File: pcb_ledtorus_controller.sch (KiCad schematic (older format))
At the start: 27 parts, among them P7 CONN_4X2, P8 CONN_9, U1 TM4C1232XXPM, U3 KNUSB, X1 NX5032GA-16MHz

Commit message: Passing ERC
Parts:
- renumbered C16 to C1, C9 to C10, C10 to C11, C11 to C12, C12 to C13, C1 to C2, C2 to C3, C3 to C4, C4 to C5, C5 to C6, C6 to C7, C7 to C8, C8 to C9, P7 to P1, P8 to P2, R6 to R1, R1 to R2, R7 to R3, R17 to R4, R8 to R5
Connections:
- net labels added: +3V3, gpio1, gpio2
- net labels removed: +3.3V, +3.3v, blank3, gnd, gsclk1, gsclk2, gsclk3, hall2, hall3, mode1, mode2, mode3, sclk3, sin2, sout2, sout3, xlat3
- wire segments 144 -> 134
- no-connect marks 1 -> 15
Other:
- moved on the sheet: B1, C1, C10, C11, C12, C13, C2, C3, C4, C5, C6, C7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

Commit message: Starting on netlist
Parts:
- B1: footprint (none) -> knielsenlib:SWITCH_FSMJSMA
- C1, C12, C13, C7, C8, C9: footprint (none) -> Capacitors_SMD:C_0805
- C10, C11, C2, C3, C4, C5, C6: footprint (none) -> Capacitors_SMD:C_0603
- D1, D2: footprint (none) -> LEDs:LED_0805
- L1: footprint (none) -> Inductors_SMD:L_0603
- P1: footprint (none) -> Pin_Headers:Pin_Header_Straight_2x04_Pitch1.27mm
- P2: footprint (none) -> Pin_Headers:Pin_Header_Straight_1x09_Pitch1.27mm
- R1, R2, R3, R4, R5: footprint (none) -> Resistors_SMD:R_0805
- U1: footprint (none) -> knielsenlib:LQFP_64
- U3: footprint (none) -> knielsenlib:10103594-0001LF
- X1: footprint (none) -> knielsenlib:NX5032GA
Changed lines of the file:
@@
 LIBS:w_device
 LIBS:pcb_ledtorus_controller-cache
-LIBS:tiva_pcb1-cache
 EELAYER 26 0
 EELAYER END
@@
 F 0 "R2" V 4630 1550 50  0000 C CNN
 F 1 "10k" V 4550 1550 40  0000 C CNN
-F 2 "" H 4550 1550 60  0001 C CNN
+F 2 "Resistors_SMD:R_0805" H 4550 1550 60  0001 C CNN
 F 3 "" H 4550 1550 60  0001 C CNN
 	1    4550 1550
@@
 F 0 "C7" H 8100 2400 50  0000 L CNN
 F 1 "10u" H 8100 2200 50  0000 L CNN
-F 2 "" H 8050 2300 60  0001 C CNN
+F 2 "Capacitors_SMD:C_0805" H 8050 2300 60  0001 C CNN
 F 3 "" H 8050 2300 60  0001 C CNN
 	1    8050 2300
@@
 F 0 "C6" H 7800 2400 50  0000 L CNN
 F 1 "100n" H 7800 2200 50  0000 L CNN
-F 2 "" H 7750 2300 60  0001 C CNN
+F 2 "Capacitors_SMD:C_0603" H 7750 2300 60  0001 C CNN
 F 3 "" H 7750 2300 60  0001 C CNN
 	1    7750 2300
@@
 F 0 "C2" H 6600 2400 50  0000 L CNN
 F 1 "100n" H 6600 2200 50  0000 L CNN
-F 2 "" H 6550 2300 60  0001 C CNN
+F 2 "Capacitors_SMD:C_0603" H 6550 2300 60  0001 C CNN
 F 3 "" H 6550 2300 60  0001 C CNN
 	1    6550 2300
@@
 F 0 "C3" H 6900 2400 50  0000 L CNN
 F 1 "100n" H 6900 2200 50  0000 L CNN
-F 2 "" H 6850 2300 60  0001 C CNN
+F 2 "Capacitors_SMD:C_0603" H 6850 2300 60  0001 C CNN
 F 3 "" H 6850 2300 60  0001 C CNN
 	1    6850 2300
@@
 F 0 "C4" H 7200 2400 50  0000 L CNN
 F 1 "100n" H 7200 2200 50  0000 L CNN
-F 2 "" H 7150 2300 60  0001 C CNN
+F 2 "Capacitors_SMD:C_0603" H 7150 2300 60  0001 C CNN
 F 3 "" H 7150 2300 60  0001 C CNN
 	1    7150 2300
@@
 F 0 "C5" H 7500 2400 50  0000 L CNN
 F 1 "100n" H 7500 2200 50  0000 L CNN
-F 2 "" H 7450 2300 60  0001 C CNN
+F 2 "Capacitors_SMD:C_0603" H 7450 2300 60  0001 C CNN
 F 3 "" H 7450 2300 60  0001 C CNN
 	1    7450 2300
@@
 F 0 "C13" H 7150 3050 50  0000 L CNN
 F 1 "2.2u" H 7150 2850 50  0000 L CNN
-F 2 "" H 7100 2950 60  0001 C CNN
+F 2 "Capacitors_SMD:C_0805" H 7100 2950 60  0001 C CNN
 F 3 "" H 7100 2950 60  0001 C CNN
 	1    7100 2950
@@
 F 0 "C12" H 6850 3050 50  0000 L CNN
 F 1 "1u" H 6850 2850 50  0000 L CNN
-F 2 "" H 6800 2950 60  0001 C CNN
+F 2 "Capacitors_SMD:C_0805" H 6800 2950 60  0001 C CNN
 F 3 "" H 6800 2950 60  0001 C CNN
 	1    6800 2950
@@
 F 0 "C11" H 6550 3050 50  0000 L CNN
 F 1 "100n" H 6550 2850 50  0000 L CNN
-F 2 "" H 6500 2950 60  0001 C CNN
+F 2 "Capacitors_SMD:C_0603" H 6500 2950 60  0001 C CNN
 F 3 "" H 6500 2950 60  0001 C CNN
 	1    6500 2950
@@
 F 0 "C10" H 6250 3050 50  0000 L CNN
 F 1 "100n" H 6250 2850 50  0000 L CNN
-F 2 "" H 6200 2950 60  0001 C CNN
+F 2 "Capacitors_SMD:C_0603" H 6200 2950 60  0001 C CNN
 F 3 "" H 6200 2950 60  0001 C CNN
 	1    6200 2950
@@
 F 0 "C9" H 4600 2800 50  0000 L CNN
 F 1 "10p" H 4600 2600 50  0000 L CNN
-F 2 "" H 4550 2700 60  0001 C CNN
+F 2 "Capacitors_SMD:C_0805" H 4550 2700 60  0001 C CNN
 F 3 "" H 4550 2700 60  0001 C CNN
 	1    4550 2700
@@
 F 0 "C8" H 4000 2800 50  0000 L CNN
 F 1 "10p" H 4000 2600 50  0000 L CNN
-F 2 "" H 3950 2700 60  0001 C CNN
+F 2 "Capacitors_SMD:C_0805" H 3950 2700 60  0001 C CNN
 F 3 "" H 3950 2700 60  0001 C CNN
 	1    3950 2700
@@
 F 0 "X1" H 4250 2350 60  0000 C CNN
 F 1 "NX5032GA-16MHz" H 4250 2050 60  0000 C CNN
-F 2 "" H 4250 2200 60  0001 C CNN
+F 2 "knielsenlib:NX5032GA" H 4250 2200 60  0001 C CNN
 F 3 "" H 4250 2200 60  0001 C CNN
 	1    4250 2200
@@
 F 0 "U1" H 5450 2700 60  0000 C CNN
 F 1 "TM4C1232XXPM" H 5450 1450 60  0000 C CNN
-F 2 "" H 5450 2150 60  0001 C CNN
+F 2 "knielsenlib:LQFP_64" H 5450 2150 60  0001 C CNN
 F 3 "" H 5450 2150 60  0001 C CNN
 	2    5450 2150
@@
 F 0 "U1" H 2250 2800 60  0000 C CNN
 F 1 "TM4C1232XXPM" H 2250 2700 60  0000 C CNN
-F 2 "" H 2250 2000 60  0000 C CNN
+F 2 "knielsenlib:LQFP_64" H 2250 2000 60  0001 C CNN
 F 3 "" H 2250 2000 60  0000 C CNN
 	1    2250 2000
@@
 F 0 "U3" H 2050 6400 60  0000 C CNN
 F 1 "KNUSB" H 2050 5700 60  0000 C CNN
-F 2 "" H 2050 6400 60  0000 C CNN
+F 2 "knielsenlib:10103594-0001LF" H 2050 6400 60  0001 C CNN
 F 3 "" H 2050 6400 60  0000 C CNN
 	1    2050 6400
@@
 F 0 "L1" V 2750 7000 40  0000 C CNN
 F 1 "30@100MHz" V 2900 7000 40  0000 C CNN
-F 2 "" H 2800 7000 60  0000 C CNN
+F 2 "Inductors_SMD:L_0603" H 2800 7000 60  0001 C CNN
 F 3 "" H 2800 7000 60  0000 C CNN
 	1    2800 7000
@@
 F 0 "B1" H 3857 1623 60  0000 C CNN
 F 1 "SWITCH_4PIN" H 3849 1145 60  0000 C CNN
-F 2 "" H 3850 1400 60  0000 C CNN
+F 2 "knielsenlib:SWITCH_FSMJSMA" H 3850 1400 60  0001 C CNN
 F 3 "" H 3850 1400 60  0000 C CNN
 	1    3850 1400
@@
 F 0 "R1" V 4630 1350 40  0000 C CNN
 F 1 "100" V 4557 1351 40  0000 C CNN
-F 2 "" V 4480 1350 30  0000 C CNN
+F 2 "Resistors_SMD:R_0805" V 4480 1350 30  0001 C CNN
 F 3 "" H 4550 1350 30  0000 C CNN
 	1    4550 1350
@@
 F 0 "C1" H 5025 1500 30  0000 L CNN
 F 1 "10n" H 5025 1400 30  0000 L CNN
-F 2 "" H 5000 1450 60  0000 C CNN
+F 2 "Capacitors_SMD:C_0805" H 5000 1450 60  0001 C CNN
 F 3 "" H 5000 1450 60  0000 C CNN
 	1    5000 1450
@@
 F 0 "R5" V 5580 4750 50  0000 C CNN
 F 1 "1k" V 5500 4750 50  0000 C CNN
-F 2 "" H 5500 4750 60  0001 C CNN
+F 2 "Resistors_SMD:R_0805" H 5500 4750 60  0001 C CNN
 F 3 "" H 5500 4750 60  0001 C CNN
 	1    5500 4750
@@
 F 0 "R3" V 5580 4300 50  0000 C CNN
 F 1 "1k" V 5500 4300 50  0000 C CNN
-F 2 "" H 5500 4300 60  0001 C CNN
+F 2 "Resistors_SMD:R_0805" H 5500 4300 60  0001 C CNN
 F 3 "" H 5500 4300 60  0001 C CNN
 	1    5500 4300
@@
 F 0 "D2" H 6150 4850 50  0000 C CNN
 F 1 "SML-211YTT86" H 6150 4650 50  0000 C CNN
-F 2 "" H 6150 4750 60  0001 C CNN
+F 2 "LEDs:LED_0805" H 6150 4750 60  0001 C CNN
 F 3 "" H 6150 4750 60  0001 C CNN
 	1    6150 4750
@@
 F 0 "D1" H 6150 4400 50  0000 C CNN
 F 1 "SML-211UTT86" H 6150 4200 50  0000 C CNN
-F 2 "" H 6150 4300 60  0001 C CNN
+F 2 "LEDs:LED_0805" H 6150 4300 60  0001 C CNN
 F 3 "" H 6150 4300 60  0001 C CNN
 	1    6150 4300
@@
 F 0 "P1" H 2400 4650 50  0000 C CNN
 F 1 "CONN_4X2" V 2400 4400 40  0000 C CNN
-F 2 "" H 2400 4400 60  0000 C CNN
+F 2 "Pin_Headers:Pin_Header_Straight_2x04_Pitch1.27mm" H 2400 4400 60  0001 C CNN
 F 3 "" H 2400 4400 60  0000 C CNN
 	1    2400 4400
@@
 F 0 "P2" V 5550 6950 60  0000 C CNN
 F 1 "CONN_9" V 5650 6950 60  0000 C CNN
-F 2 "" H 5600 6950 60  0000 C CNN
+F 2 "Pin_Headers:Pin_Header_Straight_1x09_Pitch1.27mm" H 5600 6950 60  0001 C CNN
 F 3 "" H 5600 6950 60  0000 C CNN
 	1    5600 6950
@@
 F 0 "R4" V 3480 4700 40  0000 C CNN
 F 1 "47k" V 3407 4701 40  0000 C CNN
-F 2 "" V 3330 4700 30  0000 C CNN
+F 2 "Resistors_SMD:R_0805" V 3330 4700 30  0001 C CNN
 F 3 "" H 3400 4700 30  0000 C CNN
 	1    3400 4700

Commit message: Starting on netlist
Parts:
- P1: footprint Pin_Headers:Pin_Header_Straight_2x04_Pitch1.27mm -> Pin_Headers:Pin_Header_Straight_2x04_Pitch2.54mm
- P2: footprint Pin_Headers:Pin_Header_Straight_1x09_Pitch1.27mm -> Pin_Headers:Pin_Header_Straight_1x09_Pitch2.54mm
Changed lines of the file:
@@
 LIBS:contrib
 LIBS:valves
-LIBS:w_analog
-LIBS:w_device
 LIBS:pcb_ledtorus_controller-cache
 EELAYER 26 0
@@
 F 0 "P1" H 2400 4650 50  0000 C CNN
 F 1 "CONN_4X2" V 2400 4400 40  0000 C CNN
-F 2 "Pin_Headers:Pin_Header_Straight_2x04_Pitch1.27mm" H 2400 4400 60  0001 C CNN
+F 2 "Pin_Headers:Pin_Header_Straight_2x04_Pitch2.54mm" H 2400 4400 60  0001 C CNN
 F 3 "" H 2400 4400 60  0000 C CNN
 	1    2400 4400
@@
 F 0 "P2" V 5550 6950 60  0000 C CNN
 F 1 "CONN_9" V 5650 6950 60  0000 C CNN
-F 2 "Pin_Headers:Pin_Header_Straight_1x09_Pitch1.27mm" H 5600 6950 60  0001 C CNN
+F 2 "Pin_Headers:Pin_Header_Straight_1x09_Pitch2.54mm" H 5600 6950 60  0001 C CNN
 F 3 "" H 5600 6950 60  0000 C CNN
 	1    5600 6950

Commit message: Work on layout
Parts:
- added H1, H2, H3, H4: mounting_hole, Mounting_Holes:MountingHole_4.3mm_M4, symbol mounting_hole
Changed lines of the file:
@@
 	-1   0    0    1
 $EndComp
+$Comp
+L mounting_hole H1
+U 1 1 5C292E61
+P 7450 5550
+F 0 "H1" H 7531 5605 60  0000 L CNN
+F 1 "mounting_hole" H 7531 5495 60  0000 L CNN
+F 2 "Mounting_Holes:MountingHole_4.3mm_M4" H 7450 5550 60  0001 C CNN
+F 3 "" H 7450 5550 60  0000 C CNN
+	1    7450 5550
+	1    0    0    -1
+$EndComp
+$Comp
+L mounting_hole H3
+U 1 1 5C292F44
+P 7450 5750
+F 0 "H3" H 7531 5805 60  0000 L CNN
+F 1 "mounting_hole" H 7531 5695 60  0000 L CNN
+F 2 "Mounting_Holes:MountingHole_4.3mm_M4" H 7450 5750 60  0001 C CNN
+F 3 "" H 7450 5750 60  0000 C CNN
+	1    7450 5750
+	1    0    0    -1
+$EndComp
+$Comp
+L mounting_hole H2
+U 1 1 5C292F9F
+P 7750 5550
+F 0 "H2" H 7831 5605 60  0000 L CNN
+F 1 "mounting_hole" H 7831 5495 60  0000 L CNN
+F 2 "Mounting_Holes:MountingHole_4.3mm_M4" H 7750 5550 60  0001 C CNN
+F 3 "" H 7750 5550 60  0000 C CNN
+	1    7750 5550
+	1    0    0    -1
+$EndComp
+$Comp
+L mounting_hole H4
+U 1 1 5C293020
+P 7750 5750
+F 0 "H4" H 7831 5805 60  0000 L CNN
+F 1 "mounting_hole" H 7831 5695 60  0000 L CNN
+F 2 "Mounting_Holes:MountingHole_4.3mm_M4" H 7750 5750 60  0001 C CNN
+F 3 "" H 7750 5750 60  0000 C CNN
+	1    7750 5750
+	1    0    0    -1
+$EndComp
 $EndSCHEMATC

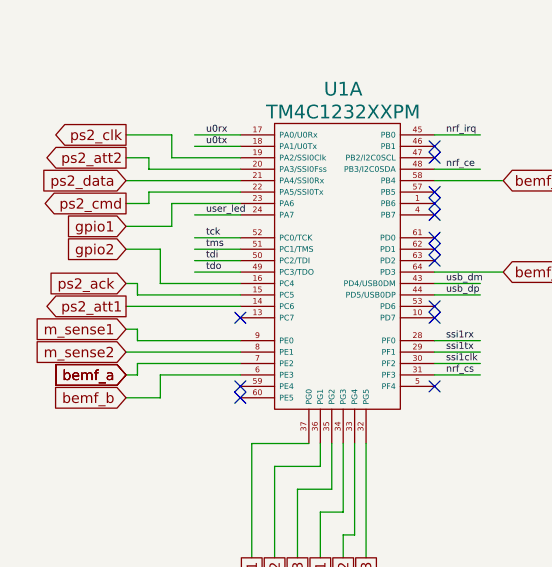
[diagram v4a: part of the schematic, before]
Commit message: Completing cleanups and ToDos:
 - L6234 thermal vias done
 - Gerbers checked
 - Misc. io and stuff tweaks
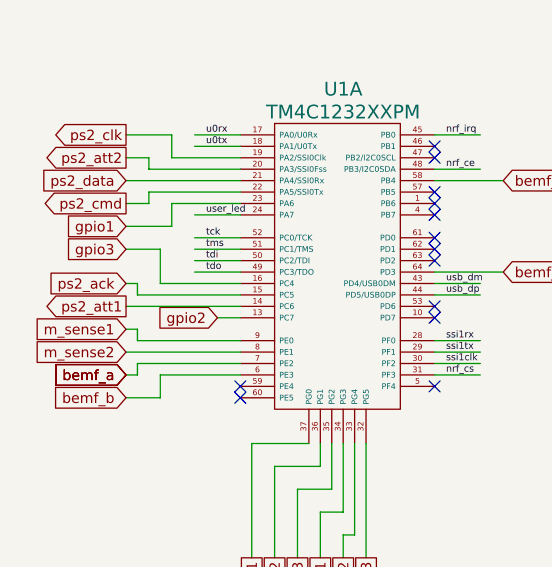
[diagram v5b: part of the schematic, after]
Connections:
- net labels added: gpio3
- wire segments 134 -> 135
- no-connect marks 15 -> 14
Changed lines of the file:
@@
 NoConn ~ 1800 2550
 NoConn ~ 1800 2500
-NoConn ~ 1800 2200
 NoConn ~ 2650 2500
 NoConn ~ 2650 2200
@@
 	1500 1800 1300 1800
 Text GLabel 1300 1900 0    45   Input ~ 0
-gpio2
+gpio3
 Wire Wire Line
 	1300 1900 1450 1900
@@
 	1    0    0    -1
 $EndComp
+Text GLabel 1700 2200 0    45   Input ~ 0
+gpio2
+Wire Wire Line
+	1700 2200 1800 2200
 $EndSCHEMATC
